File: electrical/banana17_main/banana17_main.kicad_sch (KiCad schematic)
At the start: 26 parts, among them J1 78171-0004, U1 RP2040, U2 NCP1117-3.3_SOT223, U3 ssd1306_128x32, U4 W25Q128JVS, Y1 ABMB-272-T3

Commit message: RP2040 routed.
RP2040 routed.
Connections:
- net GPIO0 renamed ROW0
- net GPIO1 renamed ROW1
- net GPIO2 renamed ROW2
- net MCU_DM renamed MCU_D+
- net MCU_DP renamed MCU_D-
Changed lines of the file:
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@@
 		)
 	)
-	(label "MCU_DP"
+	(label "MCU_D-"
 		(at 198.12 55.88 180)
 		(fields_autoplaced yes)
@@
 		)
 	)
-	(label "MCU_DM"
+	(label "MCU_D+"
 		(at 198.12 58.42 180)
 		(fields_autoplaced yes)
@@
 		)
 	)
+	(global_label "ROW1"
+		(shape input)
+		(at 265.43 50.8 0)
+		(fields_autoplaced yes)
+		(effects
+			(font
+				(size 1.27 1.27)
+			)
+			(justify left)
+		)
+		(property "Intersheetrefs" "${INTERSHEET_REFS}"
+			(at 273.6766 50.8 0)
+			(effects
+				(font
+					(size 1.27 1.27)
+				)
+				(justify left)
+				(hide yes)
+			)
+		)
+	)
 	(global_label "OLED_SDA"
 		(shape input)
@@
 		)
 	)
+	(global_label "ROW0"
+		(shape input)
+		(at 265.43 48.26 0)
+		(fields_autoplaced yes)
+		(effects
+			(font
+				(size 1.27 1.27)
+			)
+			(justify left)
+		)
+		(property "Intersheetrefs" "${INTERSHEET_REFS}"
+			(at 273.6766 48.26 0)
+			(effects
+				(font
+					(size 1.27 1.27)
+				)
+				(justify left)
+				(hide yes)
+			)
+		)
+	)
 	(global_label "OLED_GND"
 		(shape input)
@@
 				(hide yes)
 			)
+		)
+	)
+	(global_label "ROW2"
+		(shape input)
+		(at 265.43 53.34 0)
+		(fields_autoplaced yes)
+		(effects
+			(font
+				(size 1.27 1.27)
+			)
+			(justify left)
+		)
+		(property "Intersheetrefs" "${INTERSHEET_REFS}"
+			(at 273.6766 53.34 0)
+			(effects
+				(font
+					(size 1.27 1.27)
+				)
+				(justify left)
+				(hide yes)
+			)

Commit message: Incorporated USB C connector. Shrunk overall design.
Incorporated USB C connector. Shrunk overall design.
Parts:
- removed J1: 78171-0004, Connector_Molex:Molex_Pico-EZmate_78171-0004_1x04-1MP_P1.20mm_Vertical, symbol Connector_Generic_MountingPin:Conn_01x04_MountingPin
- added J2: USB_C_Receptacle_USB2.0_16P, locallib:HRO-TYPE-C-31-M-12-Assembly, symbol Connector:USB_C_Receptacle_USB2.0_16P
- added R4, R5: 5.1k, Resistor_SMD:R_0402_1005Metric_Pad0.72x0.64mm_HandSolder, symbol Device:R
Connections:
- net GND: now also J2.A1 (GND), J2.A12 (GND), J2.B1 (GND), J2.B12 (GND), J2.S1 (SHIELD), R4.2, R5.1
- net USB_D+: now also J2.A6 (D+), J2.B6 (D+)
- net USB_D-: now also J2.A7 (D-), J2.B7 (D-)
- net VBUS: now also J2.A4 (VBUS), J2.A9 (VBUS), J2.B4 (VBUS), J2.B9 (VBUS)
- new net: J2.B5 (CC2), R5.2
- new net: J2.A5 (CC1), R4.1
- no-connect marks 0 -> 2
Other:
- note added: "USB C Connector"
- note removed: "PICO Ezmate Connector (UDB)"
- moved on the sheet: U3

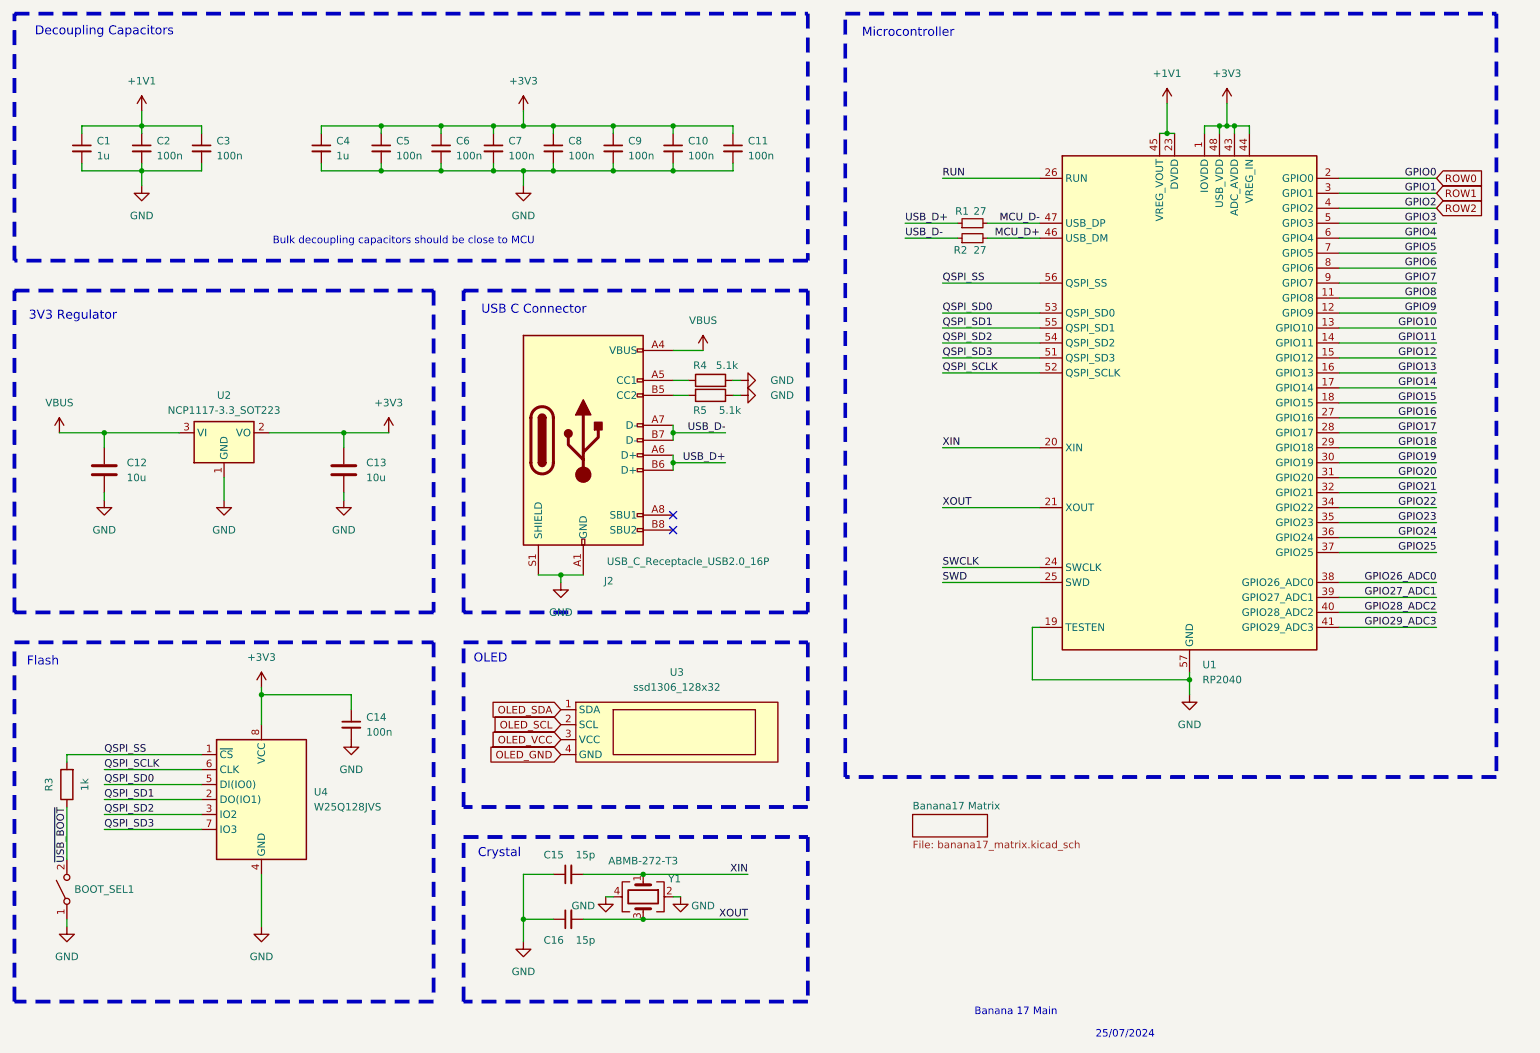
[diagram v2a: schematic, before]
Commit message: Preliminary matrix complete. Need to do encoders next.
Preliminary matrix complete. Need to do encoders next.
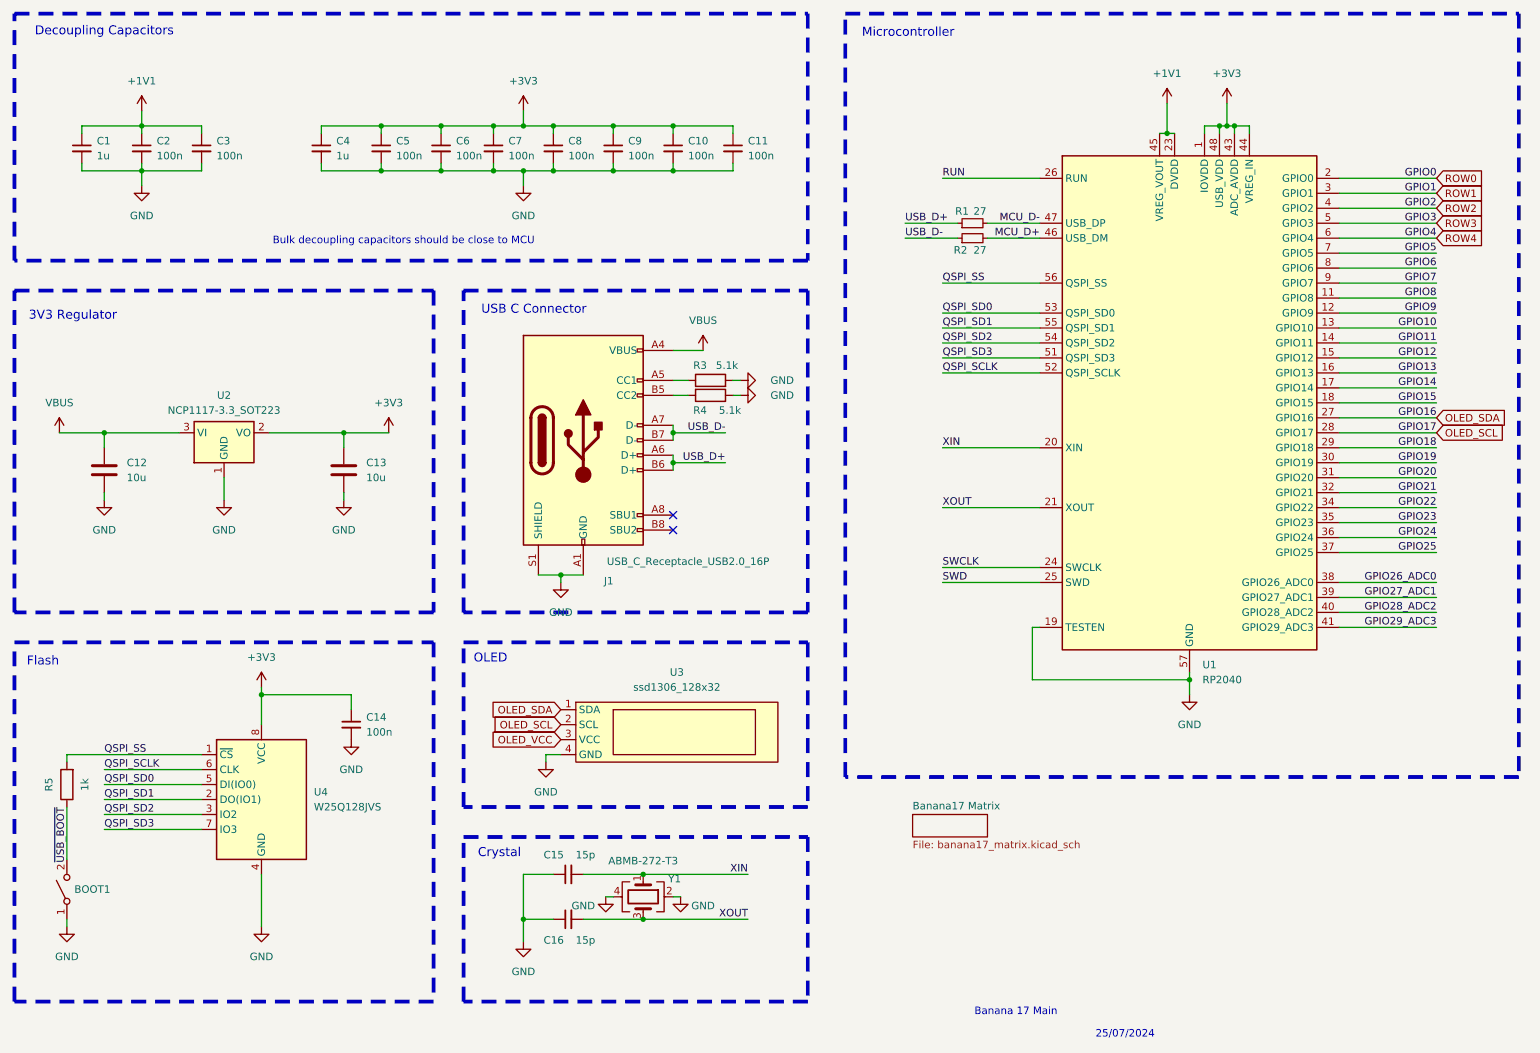
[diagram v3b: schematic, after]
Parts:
- BOOT1: renamed from BOOT_SEL1; footprint Button_Switch_SMD:SW_SPST_TL3305A -> Button_Switch_SMD:SW_SPST_PTS810
- renumbered J2 to J1, R4 to R3, R5 to R4, R3 to R5
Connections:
- net GPIO16 is gone; now on net OLED_SDA: U1.27 (GPIO16)
- net GPIO17 is gone; now on net OLED_SCL: U1.28 (GPIO17)
- net OLED_GND is gone; now on net GND: U3.4 (GND)
- net GPIO3 renamed ROW3
- net GPIO4 renamed ROW4

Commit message: Initial PCB complete.
Initial PCB complete.
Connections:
- net GPIO12 is gone; now on net OLED_SDA: U1.15 (GPIO12)
- net GPIO13 is gone; now on net OLED_SCL: U1.16 (GPIO13)
- net OLED_VCC is gone; now on net VBUS: U3.3 (VCC)
- net OLED_SCL: no longer U1.28 (GPIO17)
- net OLED_SDA: no longer U1.27 (GPIO16)
- net GPIO10 renamed ROW5
- net GPIO11 renamed COL0
- net GPIO20 renamed ENC1_A
- net GPIO21 renamed ENC1_B
- net GPIO5 renamed COL3
- net GPIO6 renamed COL4
- net GPIO9 renamed ROW6
- net ROW3 renamed COL1
- net ROW4 renamed COL2
- new net GPIO16: U1.27 (GPIO16)
- new net GPIO17: U1.28 (GPIO17)

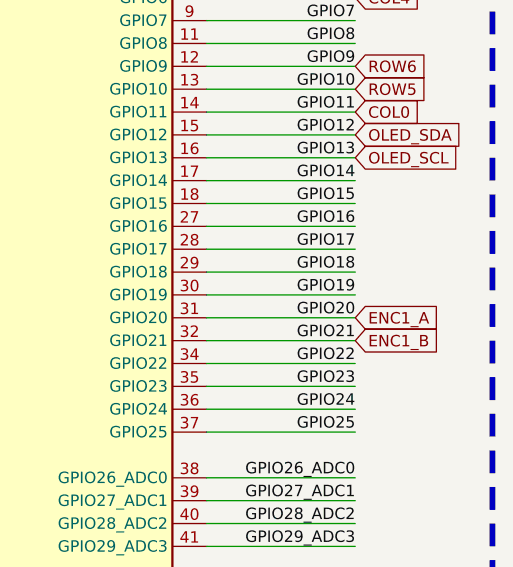
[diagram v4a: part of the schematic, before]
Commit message: Additional changes to routing from DRC.
Additional changes to routing from DRC.
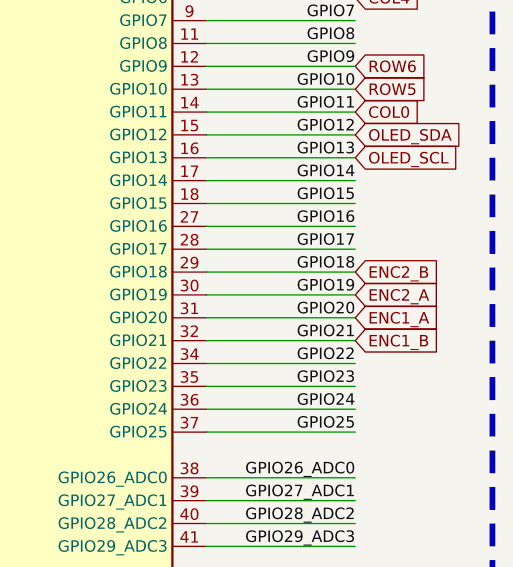
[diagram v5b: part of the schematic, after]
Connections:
- net GPIO18 renamed ENC2_B
- net GPIO19 renamed ENC2_A
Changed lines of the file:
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@@
+		)
+	)
+	(global_label "ENC2_B"
+		(shape input)
+		(at 265.43 93.98 0)
+		(fields_autoplaced yes)
+		(effects
+			(font
+				(size 1.27 1.27)
+			)
+			(justify left)
+		)
+		(property "Intersheetrefs" "${INTERSHEET_REFS}"
+			(at 275.6118 93.98 0)
+			(effects
+				(font
+					(size 1.27 1.27)
+				)
+				(justify left)
+				(hide yes)
+			)
 		)
 	)
@@
 			(effects
 				(font
+					(size 1.27 1.27)
+				)
+				(justify left)
+				(hide yes)
+			)
+		)
+	)
+	(global_label "ENC2_A"
+		(shape input)
+		(at 265.43 96.52 0)
+		(fields_autoplaced yes)
+		(effects
+			(font
+				(size 1.27 1.27)
+			)
+			(justify left)
+		)
+		(property "Intersheetrefs" "${INTERSHEET_REFS}"
+			(at 275.4304 96.52 0)
+			(effects
+				(font

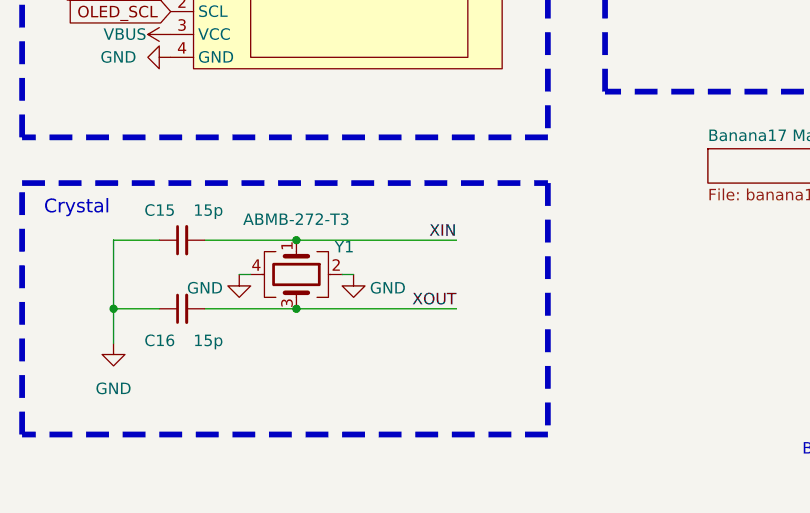
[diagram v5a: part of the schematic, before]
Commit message: Reduce PCB size less than 100mm x 100m for cheaper PCB.
Reduce PCB size less than 100mm x 100m for cheaper PCB.
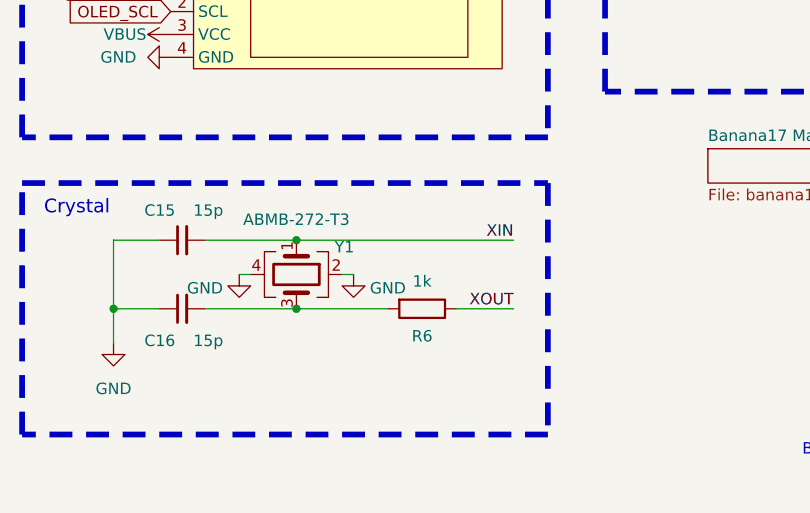
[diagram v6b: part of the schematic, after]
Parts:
- added R6: 1k, Resistor_SMD:R_0402_1005Metric_Pad0.72x0.64mm_HandSolder, symbol Device:R
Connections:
- net XOUT: now also R6.1; no longer C16.2, Y1.3
- new net: C16.2, R6.2, Y1.3
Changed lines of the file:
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@@
 	(wire
 		(pts
-			(xy 130.81 173.99) (xy 148.59 173.99)
+			(xy 130.81 173.99) (xy 140.97 173.99)
 		)
 		(stroke
@@
 	(wire
 		(pts
+			(xy 130.81 166.37) (xy 154.94 166.37)
+		)
+		(stroke
+			(width 0)
+			(type default)
+		)
+	)
+	(wire
+		(pts
 			(xy 248.92 88.9) (xy 265.43 88.9)
 		)
@@
 	(wire
 		(pts
-			(xy 130.81 166.37) (xy 148.59 166.37)
-		)
-		(stroke
-			(width 0)
-			(type default)
-		)
-	)
-	(wire
-		(pts
 			(xy 223.52 133.35) (xy 223.52 135.89)
 		)
@@
 	(wire
 		(pts
+			(xy 148.59 173.99) (xy 154.94 173.99)
+		)
+		(stroke
+			(width 0)
+			(type default)
+		)
+	)
+	(wire
+		(pts
 			(xy 248.92 119.38) (xy 265.43 119.38)
 		)
@@
 		)
 	)
+	(label "XOUT"
+		(at 154.94 173.99 180)
+		(fields_autoplaced yes)
+		(effects
+			(font
+				(size 1.27 1.27)
+			)
+			(justify right bottom)
+		)
+	)
 	(label "GPIO19"
 		(at 265.43 96.52 180)
@@
 		)
 	)
-	(label "XOUT"
-		(at 148.59 173.99 180)
-		(fields_autoplaced yes)
-		(effects
-			(font
-				(size 1.27 1.27)
-			)
-			(justify right bottom)
-		)
-	)
 	(label "GPIO3"
 		(at 265.43 55.88 180)
@@
 	)
 	(label "XIN"
-		(at 148.59 166.37 180)
+		(at 154.94 166.37 180)
 		(fields_autoplaced yes)
 		(effects
@@
 					(unit 1)
 				)
+			)
+		)
+	)
+	(symbol
+		(lib_id "Device:R")
+		(at 144.78 173.99 270)
+		(unit 1)
+		(exclude_from_sim no)
+		(in_bom yes)
+		(on_board yes)
+		(dnp no)
+		(property "Reference" "R6"
+			(at 144.78 177.038 90)
+			(effects
+				(font
+					(size 1.27 1.27)
+				)
+			)
+		)
+		(property "Value" "1k"
+			(at 144.78 170.942 90)
+			(effects
+				(font
+					(size 1.27 1.27)
+				)
+			)
+		)
+		(property "Footprint" "Resistor_SMD:R_0402_1005Metric_Pad0.72x0.64mm_HandSolder"
+			(at 144.78 172.212 90)
+			(effects
+				(font
+					(size 1.27 1.27)
+				)
+				(hide yes)
+			)
+		)
+		(property "Datasheet" "~"
+			(at 144.78 173.99 0)
+			(effects
+				(font
+					(size 1.27 1.27)
+				)
+				(hide yes)
+			)
+		)
+		(property "Description" "Resistor"
+			(at 144.78 173.99 0)
+			(effects
+				(font
+					(size 1.27 1.27)
+				)
+				(hide yes)
+			)
+		)
+		(pin "2"
+		)
+		(pin "1"
+		)
+		(instances
+			(project "banana17_main"
+				(path "/fd2b462c-d7c2-4bbf-9a41-8b3fef737a65"
+					(reference "R6")
+					(unit 1)
+				)

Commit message: Additional changes to routing.
Additional changes to routing.
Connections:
- net COL2: now also U1.4 (GPIO2); no longer U1.6 (GPIO4)
- net COL3: now also U1.3 (GPIO1); no longer U1.7 (GPIO5)
- net COL4: now also U1.2 (GPIO0); no longer U1.8 (GPIO6)
- net ROW0: now also U1.6 (GPIO4); no longer U1.2 (GPIO0)
- net ROW1: now also U1.7 (GPIO5); no longer U1.3 (GPIO1)
- net ROW2: now also U1.8 (GPIO6); no longer U1.4 (GPIO2)
- net GPIO7 renamed ROW3
- net GPIO8 renamed ROW4
- net ROW5 renamed GPIO10

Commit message: Tracks rerouted.
Tracks rerouted.
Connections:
- net GPIO10 is gone; now on net ROW3: U1.13 (GPIO10)
- net GPIO15 is gone; now on net COL0: U1.18 (GPIO15)
- net GPIO16 is gone; now on net OLED_SDA: U1.27 (GPIO16)
- net GPIO17 is gone; now on net OLED_SCL: U1.28 (GPIO17)
- net COL0: no longer U1.14 (GPIO11)
- net OLED_SCL: no longer U1.16 (GPIO13)
- net OLED_SDA: no longer U1.15 (GPIO12)
- net ROW3: no longer U1.9 (GPIO7)
- net ROW4: now also U1.14 (GPIO11); no longer U1.11 (GPIO8)
- net ROW6: now also U1.16 (GPIO13); no longer U1.12 (GPIO9)
- net GPIO14 renamed ROW5
- new net GPIO12: U1.15 (GPIO12)
- new net GPIO7: U1.9 (GPIO7)
- new net GPIO8: U1.11 (GPIO8)
- new net GPIO9: U1.12 (GPIO9)
